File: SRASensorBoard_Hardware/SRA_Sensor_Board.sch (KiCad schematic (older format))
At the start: 72 parts, among them J1 USB_A, Q1 BSS138, Q2 BSS138, Q3 BSS138, Q4 BSS138, U1 LT1910, U2 OKI, U3 OKI, U4 TM4C129E_Launchpad, U5 IRF7821PbF, U6 FT232RL

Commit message: Tracing and whatnot
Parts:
- removed Conn10: UV_LED_V+_2, MRDT_Connectors:Anderson_2_Horizontal_Stacked, symbol MRDT_Connectors:AndersonPP
- removed Conn11: UV_LED_GND, MRDT_Connectors:Anderson_2_Horizontal_Stacked, symbol MRDT_Connectors:AndersonPP
- removed Conn8: 24v Boost GND, MRDT_Connectors:Anderson_2_Horizontal_Side_by_Side, symbol MRDT_Connectors:AndersonPP
- removed Conn9: UV_LED_V+_1, MRDT_Connectors:Anderson_2_Horizontal_Stacked, symbol MRDT_Connectors:AndersonPP
- added unit 1 of Conn5
- added unit 1 of Conn6
- added unit 2 of Conn7
- added unit 3 of Conn7
- Conn5: value 12v Boost -> Boost 12V
- Conn6: value 24v Boost -> Boost 24V
- Conn7: value 12v Boost GND -> UV_led; footprint MRDT_Connectors:Anderson_2_Horizontal_Side_by_Side -> MRDT_Connectors:Anderson_3_Vertical_Side_by_Side
- R3, R4: footprint Resistor_SMD:R_0603_1608Metric_Pad1.05x0.95mm_HandSolder -> Resistor_THT:R_Axial_DIN0414_L11.9mm_D4.5mm_P15.24mm_Horizontal
- U1: footprint MRDT_ICs:SOIC127P599X175-8N -> custom:SOIC127P599X175-8N
- U5: footprint MRDT_ICs:IRF7821PBF -> custom:IRF7821PBF
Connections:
- net labels removed: C02_In, C02_Out, Flow_Output, Flow_Receive
- wire segments 184 -> 185
- no-connect marks 71 -> 70
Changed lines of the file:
@@
 NoConn ~ 11950 1450
 NoConn ~ 11950 1350
-NoConn ~ 11950 1250
 NoConn ~ 11050 1150
 NoConn ~ 11050 1250
@@
 $EndComp
 Text GLabel 9150 1350 0    50   Input ~ 0
-C02_In
+TIVA_CO2_RX
 Wire Wire Line
 	9150 1350 9250 1350
 Text GLabel 9150 1450 0    50   Output ~ 0
-C02_Out
+TIVA_CO2_TX
 Wire Wire Line
 	9150 1450 9250 1450
@@
 	9250 1850 9150 1850
 Text GLabel 10300 3050 2    50   Input ~ 0
-Flow_Receive
+TIVA_O2_RX
 Wire Wire Line
 	10300 3050 10150 3050
 Text GLabel 10300 3150 2    50   Output ~ 0
-Flow_Output
+TIVA_O2_TX
 Wire Wire Line
 	10300 3150 10150 3150
@@
 	7300 2150 7250 2150
 $Comp
-L MRDT_Connectors:AndersonPP Conn11
-U 1 1 5E0678B6
-P 5050 8750
-F 0 "Conn11" H 5258 9137 60  0000 C CNN
-F 1 "UV_LED_GND" H 5258 9031 60  0000 C CNN
-F 2 "MRDT_Connectors:Anderson_2_Horizontal_Stacked" H 4900 8200 60  0001 C CNN
-F 3 "" H 4900 8200 60  0001 C CNN
-	1    5050 8750
-	-1   0    0    -1
-$EndComp
-$Comp
-L MRDT_Connectors:AndersonPP Conn9
-U 2 1 5E06AAF7
-P 5050 7850
-F 0 "Conn9" H 5258 8237 60  0000 C CNN
-F 1 "UV_LED_V+_1" H 5258 8131 60  0000 C CNN
-F 2 "MRDT_Connectors:Anderson_2_Horizontal_Stacked" H 4900 7300 60  0001 C CNN
-F 3 "" H 4900 7300 60  0001 C CNN
-	2    5050 7850
-	-1   0    0    -1
-$EndComp
-$Comp
-L MRDT_Connectors:AndersonPP Conn10
-U 2 1 5E06CBB0
-P 5050 8300
-F 0 "Conn10" H 5258 8687 60  0000 C CNN
-F 1 "UV_LED_V+_2" H 5258 8581 60  0000 C CNN
-F 2 "MRDT_Connectors:Anderson_2_Horizontal_Stacked" H 4900 7750 60  0001 C CNN
-F 3 "" H 4900 7750 60  0001 C CNN
-	2    5050 8300
-	-1   0    0    -1
-$EndComp
-$Comp
 L Device:R R3
 U 1 1 5E06E706
@@
 F 0 "R3" V 4300 7750 50  0000 C CNN
 F 1 "4" V 4400 7750 50  0000 C CNN
-F 2 "Resistor_SMD:R_0603_1608Metric_Pad1.05x0.95mm_HandSolder" V 4330 7750 50  0001 C CNN
+F 2 "Resistor_THT:R_Axial_DIN0414_L11.9mm_D4.5mm_P15.24mm_Horizontal" V 4330 7750 50  0001 C CNN
 F 3 "~" H 4400 7750 50  0001 C CNN
 	1    4400 7750
@@
 F 0 "R4" V 4300 8200 50  0000 C CNN
 F 1 "4" V 4400 8200 50  0000 C CNN
-F 2 "Resistor_SMD:R_0603_1608Metric_Pad1.05x0.95mm_HandSolder" V 4330 8200 50  0001 C CNN
+F 2 "Resistor_THT:R_Axial_DIN0414_L11.9mm_D4.5mm_P15.24mm_Horizontal" V 4330 8200 50  0001 C CNN
 F 3 "~" H 4400 8200 50  0001 C CNN
 	1    4400 8200
@@
 Wire Wire Line
 	4500 8650 4650 8650
-$Comp
-L MRDT_Connectors:AndersonPP Conn5
-U 2 1 5E105269
-P 1650 6400
-F 0 "Conn5" H 1858 6787 60  0000 C CNN
-F 1 "12v Boost" H 1858 6681 60  0000 C CNN
-F 2 "MRDT_Connectors:Anderson_2_Horizontal_Side_by_Side" H 1500 5850 60  0001 C CNN
-F 3 "" H 1500 5850 60  0001 C CNN
-	2    1650 6400
-	1    0    0    -1
-$EndComp
-$Comp
-L MRDT_Connectors:AndersonPP Conn6
-U 2 1 5E1058D4
-P 1650 6850
-F 0 "Conn6" H 1858 7237 60  0000 C CNN
-F 1 "24v Boost" H 1858 7131 60  0000 C CNN
-F 2 "MRDT_Connectors:Anderson_2_Horizontal_Side_by_Side" H 1500 6300 60  0001 C CNN
-F 3 "" H 1500 6300 60  0001 C CNN
-	2    1650 6850
-	1    0    0    -1
-$EndComp
-$Comp
-L MRDT_Connectors:AndersonPP Conn7
-U 1 1 5E1070D1
-P 2500 6400
-F 0 "Conn7" H 2708 6787 60  0000 C CNN
-F 1 "12v Boost GND" H 2708 6681 60  0000 C CNN
-F 2 "MRDT_Connectors:Anderson_2_Horizontal_Side_by_Side" H 2350 5850 60  0001 C CNN
-F 3 "" H 2350 5850 60  0001 C CNN
-	1    2500 6400
-	1    0    0    -1
-$EndComp
 Wire Wire Line
 	3050 6300 2900 6300
-$Comp
-L MRDT_Connectors:AndersonPP Conn8
-U 1 1 5E112038
-P 2500 6850
-F 0 "Conn8" H 2708 7237 60  0000 C CNN
-F 1 "24v Boost GND" H 2708 7131 60  0000 C CNN
-F 2 "MRDT_Connectors:Anderson_2_Horizontal_Side_by_Side" H 2350 6300 60  0001 C CNN
-F 3 "" H 2350 6300 60  0001 C CNN
-	1    2500 6850
-	1    0    0    -1
-$EndComp
 Wire Wire Line
 	3050 6300 3050 6750
@@
 F 0 "U5" H 4100 7613 60  0000 C CNN
 F 1 "IRF7821PbF" H 4100 7719 60  0000 C CNN
-F 2 "MRDT_ICs:IRF7821PBF" H 3750 7800 60  0001 C CNN
+F 2 "custom:IRF7821PBF" H 3750 7800 60  0001 C CNN
 F 3 "" H 3750 7800 60  0001 C CNN
 	1    3750 7800
@@
 F 0 "U1" H 2075 8937 60  0000 C CNN
 F 1 "LT1910" H 2075 8831 60  0000 C CNN
-F 2 "MRDT_ICs:SOIC127P599X175-8N" H 1700 8250 60  0001 C CNN
+F 2 "custom:SOIC127P599X175-8N" H 1700 8250 60  0001 C CNN
 F 3 "" H 1700 8250 60  0001 C CNN
 	1    1700 8250
@@
 Connection ~ 3950 7950
 Connection ~ 3950 7850
-$Comp
-L power:+12V #PWR0142
-U 1 1 5DEF9EB2
-P 2850 7700
-F 0 "#PWR0142" H 2850 7550 50  0001 C CNN
-F 1 "+12V" H 2865 7873 50  0000 C CNN
-F 2 "" H 2850 7700 50  0001 C CNN
-F 3 "" H 2850 7700 50  0001 C CNN
-	1    2850 7700
-	1    0    0    -1
-$EndComp
 Wire Wire Line
 	2850 7700 2850 7850
@@
 	1    0    0    -1
 $EndComp
+$Comp
+L MRDT_Connectors:AndersonPP Conn5
+U 1 1 5DF191BA
+P 2500 6400
+F 0 "Conn5" H 2708 6787 60  0000 C CNN
+F 1 "Boost 12V" H 2708 6681 60  0000 C CNN
+F 2 "MRDT_Connectors:Anderson_2_Horizontal_Side_by_Side" H 2350 5850 60  0001 C CNN
+F 3 "" H 2350 5850 60  0001 C CNN
+	1    2500 6400
+	1    0    0    -1
+$EndComp
+$Comp
+L MRDT_Connectors:AndersonPP Conn5
+U 2 1 5DF1A3DD
+P 1650 6400
+F 0 "Conn5" H 1858 6787 60  0000 C CNN
+F 1 "Boost 12V" H 1858 6681 60  0000 C CNN
+F 2 "MRDT_Connectors:Anderson_2_Horizontal_Side_by_Side" H 1500 5850 60  0001 C CNN
+F 3 "" H 1500 5850 60  0001 C CNN
+	2    1650 6400
+	1    0    0    -1
+$EndComp
+$Comp
+L MRDT_Connectors:AndersonPP Conn6
+U 1 1 5DF1BFA3
+P 2500 6850
+F 0 "Conn6" H 2708 7237 60  0000 C CNN
+F 1 "Boost 24V" H 2708 7131 60  0000 C CNN
+F 2 "MRDT_Connectors:Anderson_2_Horizontal_Side_by_Side" H 2350 6300 60  0001 C CNN
+F 3 "" H 2350 6300 60  0001 C CNN
+	1    2500 6850
+	1    0    0    -1
+$EndComp
+$Comp
+L MRDT_Connectors:AndersonPP Conn6
+U 2 1 5DF1D6EB
+P 1650 6850
+F 0 "Conn6" H 1858 7237 60  0000 C CNN
+F 1 "Boost 24V" H 1858 7131 60  0000 C CNN
+F 2 "MRDT_Connectors:Anderson_2_Horizontal_Side_by_Side" H 1500 6300 60  0001 C CNN
+F 3 "" H 1500 6300 60  0001 C CNN
+	2    1650 6850
+	1    0    0    -1
+$EndComp
+$Comp
+L MRDT_Connectors:AndersonPP Conn7
+U 2 1 5DF2AC04
+P 5050 7650
+F 0 "Conn7" H 5022 7697 60  0000 R CNN
+F 1 "UV_led" H 5022 7803 60  0000 R CNN
+F 2 "MRDT_Connectors:Anderson_3_Vertical_Side_by_Side" H 4900 7100 60  0001 C CNN
+F 3 "" H 4900 7100 60  0001 C CNN
+	2    5050 7650
+	-1   0    0    1
+$EndComp
+$Comp
+L MRDT_Connectors:AndersonPP Conn7
+U 3 1 5DF2D162
+P 5050 8100
+F 0 "Conn7" H 5022 8147 60  0000 R CNN
+F 1 "UV_led" H 5022 8253 60  0000 R CNN
+F 2 "MRDT_Connectors:Anderson_3_Vertical_Side_by_Side" H 4900 7550 60  0001 C CNN
+F 3 "" H 4900 7550 60  0001 C CNN
+	3    5050 8100
+	-1   0    0    1
+$EndComp
+$Comp
+L MRDT_Connectors:AndersonPP Conn7
+U 1 1 5DF2E03B
+P 5050 8550
+F 0 "Conn7" H 5022 8597 60  0000 R CNN
+F 1 "UV_led" H 5022 8703 60  0000 R CNN
+F 2 "MRDT_Connectors:Anderson_3_Vertical_Side_by_Side" H 4900 8000 60  0001 C CNN
+F 3 "" H 4900 8000 60  0001 C CNN
+	1    5050 8550
+	-1   0    0    1
+$EndComp
+Text GLabel 12000 1250 2    50   Output ~ 0
+Reset
+Wire Wire Line
+	12000 1250 11950 1250
+$Comp
+L power:+24V #PWR?
+U 1 1 5DF80D2F
+P 2850 7700
+F 0 "#PWR?" H 2850 7550 50  0001 C CNN
+F 1 "+24V" H 2865 7873 50  0000 C CNN
+F 2 "" H 2850 7700 50  0001 C CNN
+F 3 "" H 2850 7700 50  0001 C CNN
+	1    2850 7700
+	1    0    0    -1
+$EndComp

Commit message: Added Gerbs and whatnot
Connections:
- net labels removed: USB_RX, USB_TX
- wire segments 185 -> 183
- no-connect marks 70 -> 72
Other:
- note added: "O2 Sensor"
- note removed: "Flow Sensor"
- note removed: "Telaire T6613"
- moved on the sheet: Conn5A, Conn5B, Conn6A, Conn6B, Conn7A, Conn7B, Conn7C, D10, D16, D17, D5, D6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

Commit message: PRR Changes
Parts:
- removed U1: LT1910, custom:SOIC127P599X175-8N, symbol MRDT_ICs:LT1910
- removed U5: IRF7821PbF, custom:IRF7821PBF, symbol MRDT_ICs:IRF7821PbF
- added Q5: Q_PMOS_GDS, Package_TO_SOT_SMD:TO-252-2, symbol Device:Q_PMOS_GDS
- added Q6: Q_NMOS_GSD, Package_TO_SOT_SMD:SOT-23, symbol Device:Q_NMOS_GSD
- added R28, R29: 22k, Resistor_SMD:R_0603_1608Metric_Pad1.05x0.95mm_HandSolder, symbol Device:R
- added R30: 10k, Resistor_SMD:R_0603_1608Metric_Pad1.05x0.95mm_HandSolder, symbol Device:R
- R11, R12, R13, R14, R15, R16, R17, R18, R19, R20, R23, R24, R7: value 510 -> 330
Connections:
- wire segments 183 -> 201
- no-connect marks 72 -> 70
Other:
- note added: "INPUT"
- note added: "Methane Sensor USB A\n"
- note added: "OUTPUT"
- note added: "Off Board Boost Converter"
- note added: "PINK"
- note added: "PINK\n"
- note added: "Serial 4"
- note added: "Serial 5"
- note added: "Serial 7"
- note removed: "Boost Converter"
- moved on the sheet: Conn5A, Conn5B, Conn6A, Conn6B, Conn7A, Conn7B, Conn7C, D10, D11, D12, D13, D14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

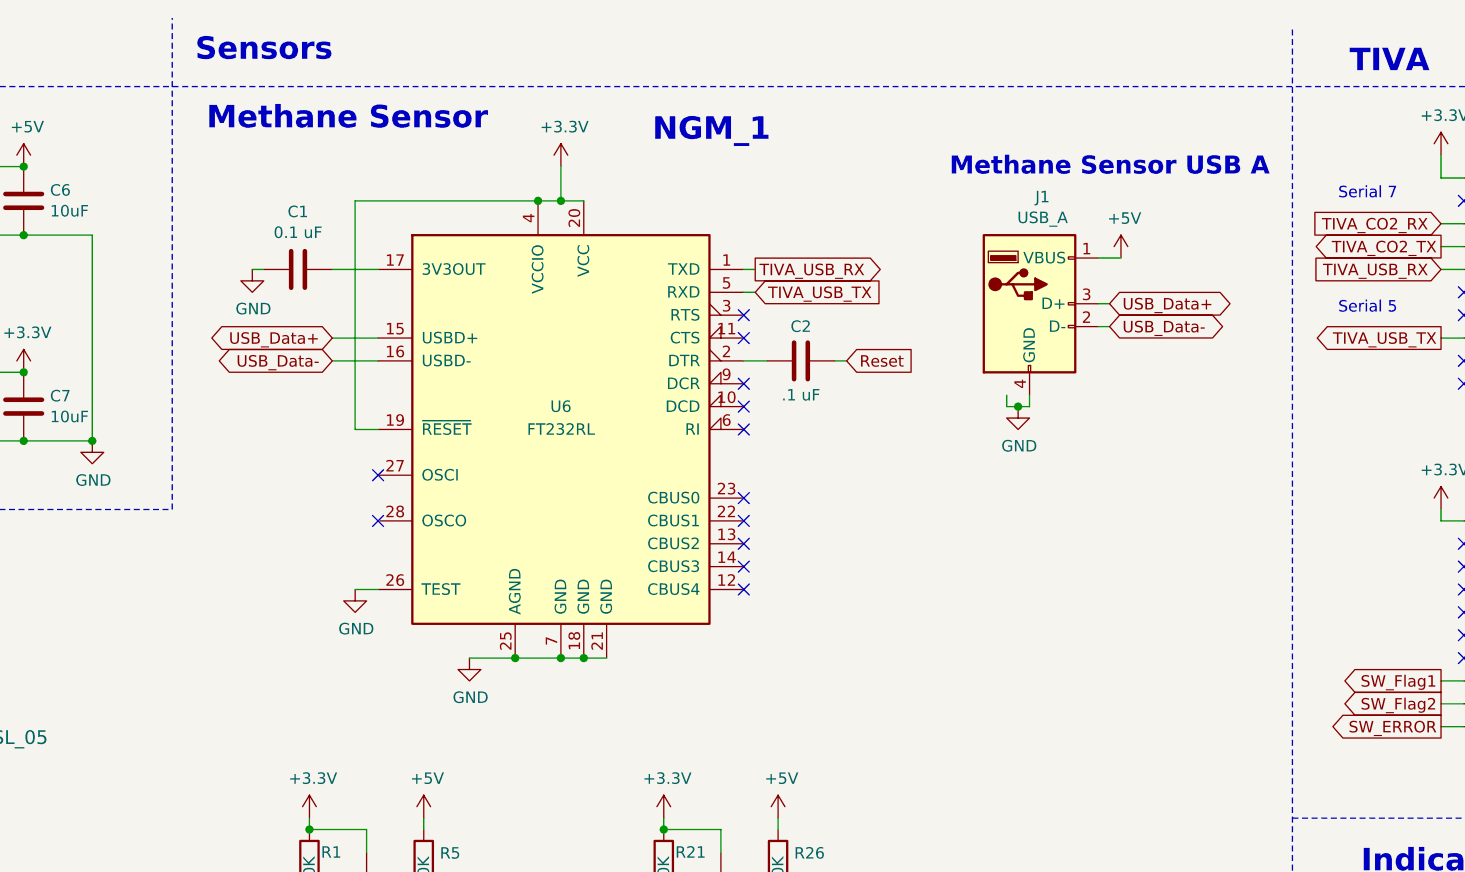
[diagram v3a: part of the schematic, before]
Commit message: Rev 2
Changed to a FT230XS due to communication problems.
Moved the power resistors because they looked a little to close to
microcontroller components.
Made some labels more visible.
Changed the footprint for the usb to be correct with the component.
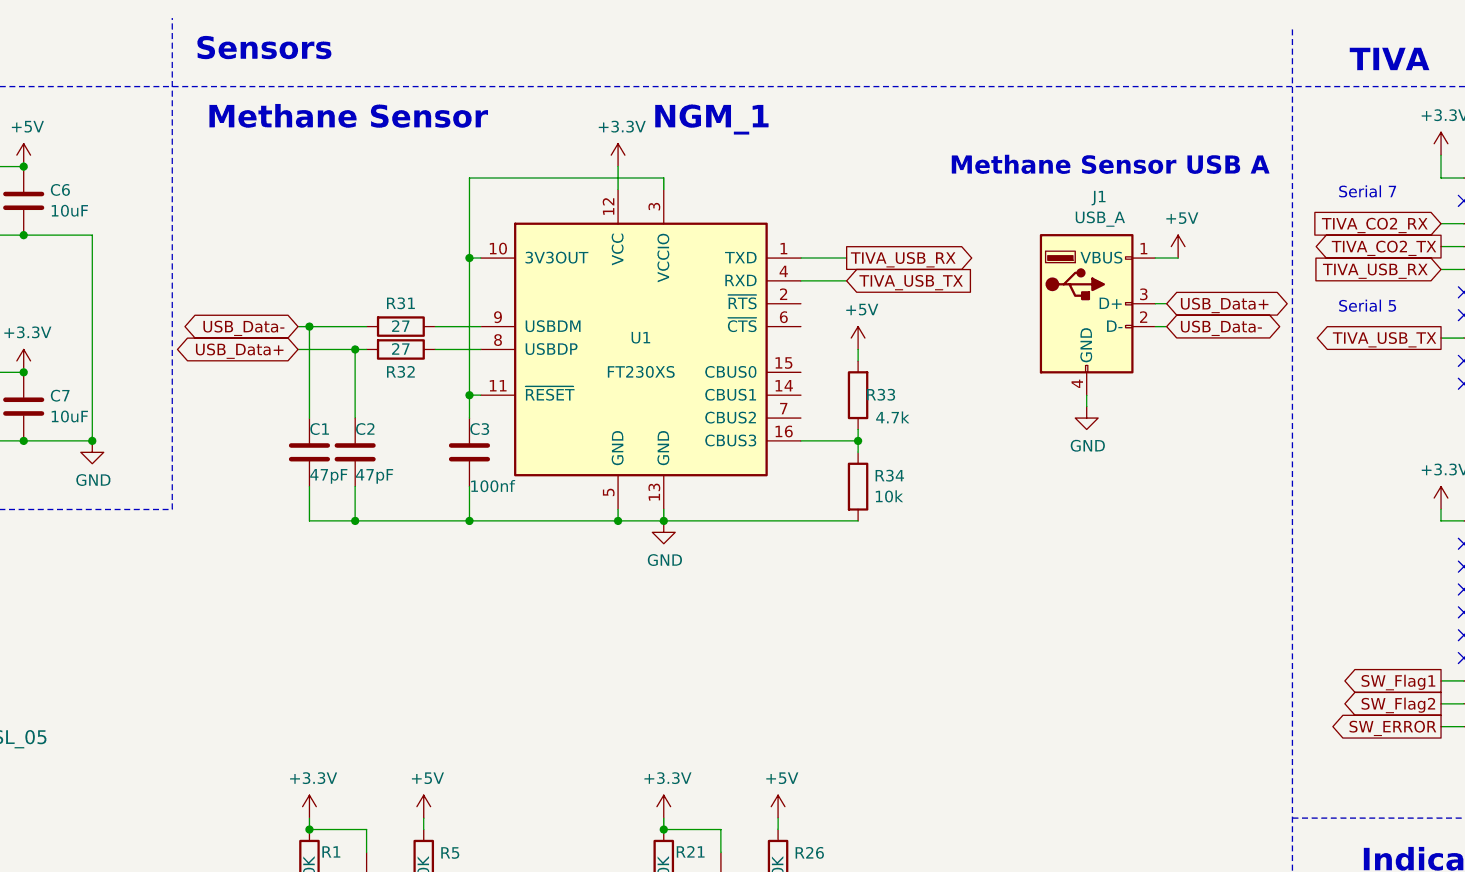
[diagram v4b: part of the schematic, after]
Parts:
- removed U6: FT232RL, Package_SO:SSOP-28_5.3x10.2mm_P0.65mm, symbol Interface_USB:FT232RL
- added C3: 100nf, Capacitor_SMD:C_0603_1608Metric_Pad1.05x0.95mm_HandSolder, symbol Device:C
- added R31, R32: 27, Resistor_SMD:R_0603_1608Metric_Pad1.05x0.95mm_HandSolder, symbol Device:R
- added R33: 4.7k, Resistor_SMD:R_0603_1608Metric_Pad1.05x0.95mm_HandSolder, symbol Device:R
- added R34: 10k, Resistor_SMD:R_0603_1608Metric_Pad1.05x0.95mm_HandSolder, symbol Device:R
- added U1: FT230XS, Package_SO:SSOP-16_3.9x4.9mm_P0.635mm, symbol Interface_USB:FT230XS
- C1: value 0.1 uF -> 47pF
- C2: value .1 uF -> 47pF
- Conn7: footprint MRDT_Connectors:Anderson_3_Vertical_Side_by_Side -> MRDT_Connectors:Anderson_3_Horizontal_Side_by_Side
- J1: footprint Connector_USB:USB3_A_Molex_48393-001 -> custom:292303-1
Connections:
- net +3V3: now also U1.12 (VCC)
- net +5V: now also R33.2
- net GND: now also C2.2, C3.2, R34.2, U1.13 (GND), U1.5 (GND)
- net Reset: no longer C2.1
- net TIVA_USB_RX: now also U1.1 (TXD)
- net TIVA_USB_TX: now also U1.4 (RXD)
- net USB_Data+: now also C2.1, R32.2
- net USB_Data-: now also C1.1, R31.2
- new net: C3.1, U1.10 (3V3OUT), U1.11 (~RESET), U1.3 (VCCIO)
- new net: R33.1, R34.1, U1.16 (CBUS3)
- new net: R32.1, U1.8 (USBDP)
- new net: R31.1, U1.9 (USBDM)
- no-connect marks 70 -> 58
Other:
- moved on the sheet: J1

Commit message: Rev 2 prt 2 changes
Updated UV led to current format
Removed CCD
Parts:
- removed Conn4: Molex_SL_05, MRDT_Connectors:MOLEX_SL_05_Vertical, symbol MRDT_Connectors:Molex_SL_05
- removed unit 3 of Conn7
- removed D12, D13, D14: LED, Diode_SMD:D_0603_1608Metric_Pad1.05x0.95mm_HandSolder, symbol Device:LED
- removed R18, R19, R20: 330, Resistor_SMD:R_0603_1608Metric_Pad1.05x0.95mm_HandSolder, symbol Device:R
- removed R4: 4, Resistor_THT:R_Axial_DIN0414_L11.9mm_D4.5mm_P15.24mm_Horizontal, symbol Device:R
- Conn7: footprint MRDT_Connectors:Anderson_3_Horizontal_Side_by_Side -> MRDT_Connectors:Anderson_2_Horizontal_Side_by_Side
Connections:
- net CCD_INT1: no longer names the net of U4.PE0 (B1_3)
- net CCD_INT2: no longer names the net of U4.PE1 (B1_4)
- net CCD_OS: no longer names the net of U4.PK3 (B2_8)
- no-connect marks 58 -> 61
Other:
- note removed: "CCD_TIVA"
- note removed: "YELLO\n"
- moved on the sheet: Conn7A, Conn7B, R3

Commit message: new sensor rev 2
moved to hierarchy and added new power circuits
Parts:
- removed C1, C2: 47pF, Capacitor_SMD:C_0603_1608Metric_Pad1.05x0.95mm_HandSolder, symbol Device:C
- removed C3: 100nf, Capacitor_SMD:C_0603_1608Metric_Pad1.05x0.95mm_HandSolder, symbol Device:C
- removed C4, C5, C6, C7: 10uF, Capacitor_SMD:C_0603_1608Metric_Pad1.05x0.95mm_HandSolder, symbol Device:C
- removed Conn1, Conn3: Molex_SL_04, MRDT_Connectors:MOLEX_SL_04_Vertical, symbol MRDT_Connectors:Molex_SL_04
- removed Conn2: AndersonPP, MRDT_Connectors:Anderson_2_Horizontal_Side_by_Side, symbol MRDT_Connectors:AndersonPP
- removed Conn5: Boost 12V, MRDT_Connectors:Anderson_2_Horizontal_Side_by_Side, symbol MRDT_Connectors:AndersonPP
- removed Conn6: Boost 24V, MRDT_Connectors:Anderson_2_Horizontal_Side_by_Side, symbol MRDT_Connectors:AndersonPP
- removed Conn7: UV_led, MRDT_Connectors:Anderson_2_Horizontal_Side_by_Side, symbol MRDT_Connectors:AndersonPP
- removed J1: USB_A, custom:292303-1, symbol Connector:USB_A
- removed Q1, Q2, Q3, Q4: BSS138, Package_TO_SOT_SMD:SOT-23, symbol Transistor_FET:BSS138
- removed Q5: Q_PMOS_GDS, Package_TO_SOT_SMD:TO-252-2, symbol Device:Q_PMOS_GDS
- removed Q6: Q_NMOS_GSD, Package_TO_SOT_SMD:SOT-23, symbol Device:Q_NMOS_GSD
- removed R1, R2, R21, R25, R26, R27, R5, R6: 10K, Resistor_SMD:R_0603_1608Metric_Pad1.05x0.95mm_HandSolder, symbol Device:R
- removed R28, R29: 22k, Resistor_SMD:R_0603_1608Metric_Pad1.05x0.95mm_HandSolder, symbol Device:R
- removed R3: 4, Resistor_THT:R_Axial_DIN0414_L11.9mm_D4.5mm_P15.24mm_Horizontal, symbol Device:R
- removed R30, R34: 10k, Resistor_SMD:R_0603_1608Metric_Pad1.05x0.95mm_HandSolder, symbol Device:R
- removed R31, R32: 27, Resistor_SMD:R_0603_1608Metric_Pad1.05x0.95mm_HandSolder, symbol Device:R
- removed R33: 4.7k, Resistor_SMD:R_0603_1608Metric_Pad1.05x0.95mm_HandSolder, symbol Device:R
- removed U1: FT230XS, Package_SO:SSOP-16_3.9x4.9mm_P0.635mm, symbol Interface_USB:FT230XS
- removed U2, U3: OKI, MRDT_Devices:OKI_Horizontal, symbol MRDT_Devices:OKI
- removed U4: TM4C129E_Launchpad, MRDT_Shields:TM4C129E_Launchpad_FULL_THT_BOTTOM, symbol SRA_Sensor_Board-rescue:TM4C129E_Launchpad-MRDT_Shields-SRA_Sensor_Board-rescue
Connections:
- no-connect marks 61 -> 0
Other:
- note added: "SICENCE SENSOR BOARD REV2"
- note removed: "CO2_Sensor\n"
- note removed: "INPUT"
- note removed: "Methane Sensor"
- note removed: "Methane Sensor USB A\n"
- note removed: "NGM_1"
- note removed: "O2 Sensor"
- note removed: "OUTPUT"
- note removed: "Off Board Boost Converter"
- note removed: "Power\n"
- note removed: "Sensors\n"
- note removed: "Serial 4"
- note removed: "Serial 5"
- note removed: "Serial 7"
- note removed: "TIVA"
- note removed: "UV_LED"
- moved on the sheet: D10, D11, D15, D16, D17, D18, D2, D3, D4, D5, D6, D7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
